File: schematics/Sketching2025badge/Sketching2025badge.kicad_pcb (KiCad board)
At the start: 2 copper layers, 100 x 100 mm, 47 parts, among them J1 Conn_02x03, J2 Conn_01x04_Pin, SW1 Capacitive_Button, SW10 SSSS811101, SW2 Capacitive_Button, SW3 Capacitive_Button, U1 ATtiny816-M

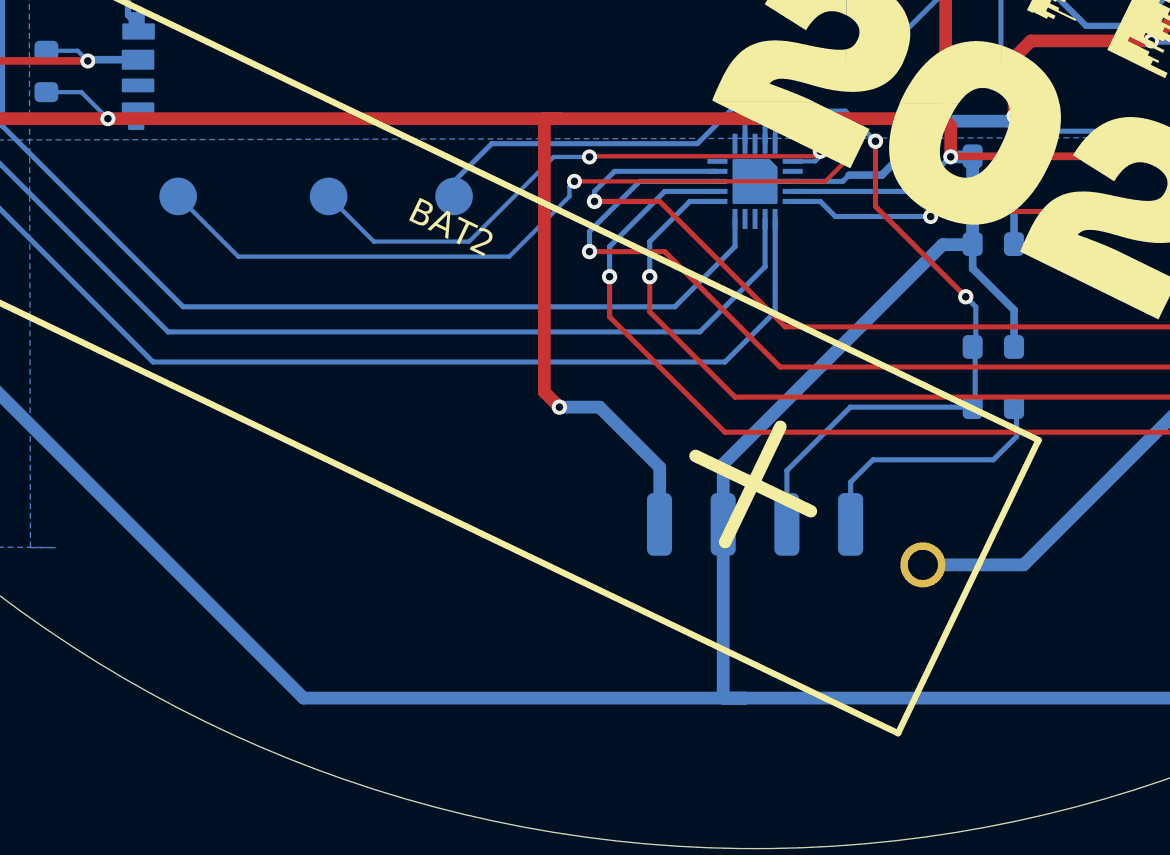
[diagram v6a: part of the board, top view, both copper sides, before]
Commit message: moved to female prog header, widened mask polygons for more light
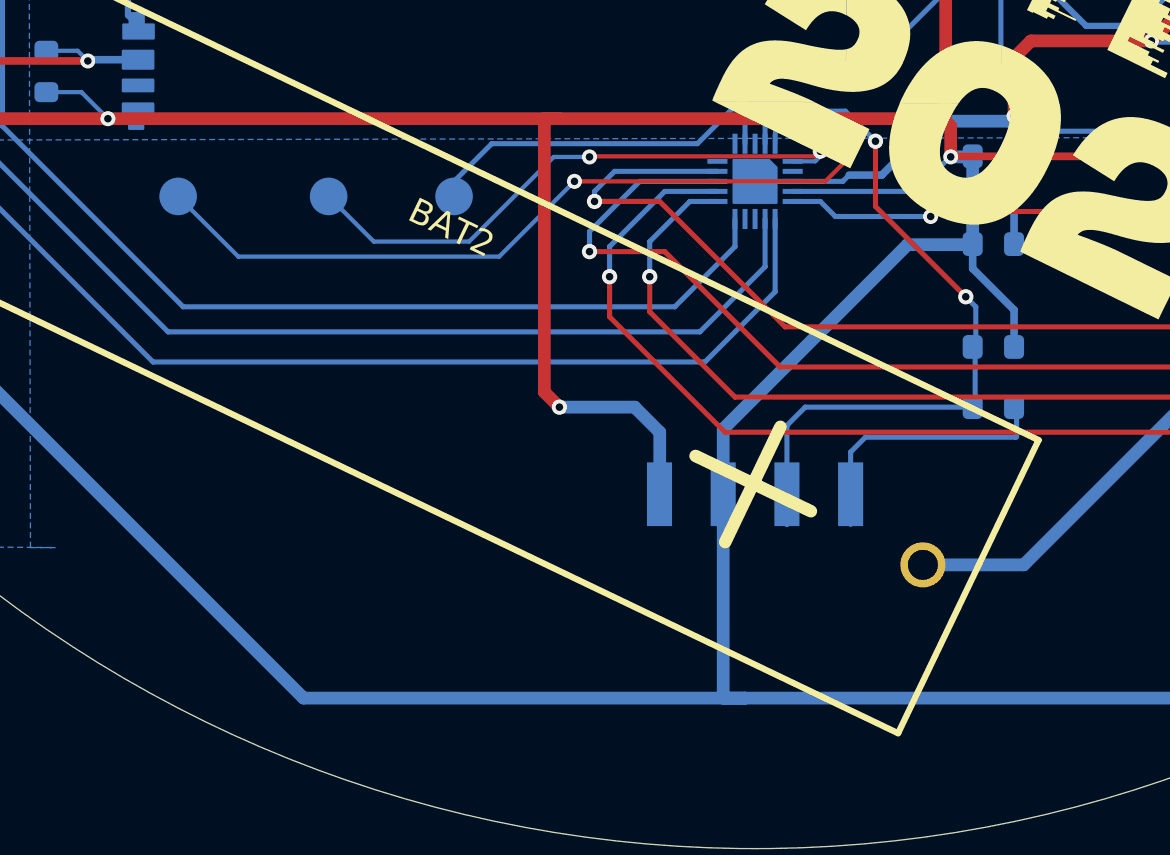
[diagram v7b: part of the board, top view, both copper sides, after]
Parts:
- removed J2: Conn_01x04_Pin, Connector_Harwin:Harwin_M20-89004xx_1x04_P2.54mm_Horizontal
- added CN1: X6511FRS-04-C85D30, easyeda2kicad:HDR-SMD_4P-P2.54-H-F, B.Cu at (100.0, 135.9)
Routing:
- net /RESET: track 28.6 -> 29.6 mm
- net VCC: track 458.6 -> 459.4 mm
- net /TX: track 10.2 -> 10.9 mm
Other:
- board text added: "tx rx V+ gnd"
- board text removed: "tx rx 3v3 gnd"

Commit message: minor fixups to pcb
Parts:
- moved LED9 4.86 mm to (76.2, 114.2)
- moved C11 4.59 mm to (73.0, 114.6)
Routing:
- net GND: track 406.9 -> 412.4 mm
- net Net-(LED8-DOUT): track 26.9 -> 21.7 mm
- net VCC: track 459.4 -> 458.5 mm
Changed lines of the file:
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@@
 	(footprint "todbot_stuff:LED-SMD_4P-L4.0-W1.6-L"
 		(layer "B.Cu")
-		(at 75.4125 119 -90)
+		(at 76.2 114.2 -90)
 		(property "Reference" "LED9"
 			(at 3.2 0.4125 180)
@@
 	(footprint "Resistor_SMD:R_0603_1608Metric"
 		(layer "B.Cu")
-		(at 71.745843 119.018187 -90)
+		(at 73 114.6 -90)
 		(descr "Resistor SMD 0603 (1608 Metric), square (rectangular) end terminal, IPC-7351 nominal, (Body size source: IPC-SM-782 page 72, https://www.pcb-3d.com/wordpress/wp-content/uploads/ipc-sm-782a_amendment_1_and_2.pdf), generated with kicad-footprint-generator")
 		(tags "resistor")
@@
 	)
 	(gr_rect
-		(start 76.9 117.4)
-		(end 97.9 120.4)
+		(start 77.3 112.6)
+		(end 97.9 115.6)
 		(stroke
 			(width 0.1)
@@
 	)
 	(segment
-		(start 92.2 120.9)
-		(end 74.2 120.9)
-		(width 0.508)
-		(layer "F.Cu")
-		(net 1)
-	)
-	(segment
 		(start 94.6 104)
 		(end 94.6 106.4)
@@
 	)
 	(segment
+		(start 92.2 120.9)
+		(end 75.4 120.9)
+		(width 0.508)
+		(layer "F.Cu")
+		(net 1)
+	)
+	(segment
 		(start 106 96.8)
 		(end 101.8 92.6)
@@
 	)
 	(segment
-		(start 92.2 120.9)
-		(end 106.19575 120.9)
+		(start 67.527876 120.9)
+		(end 65.656566 119.02869)
 		(width 0.508)
 		(layer "F.Cu")
@@
 	)
 	(segment
-		(start 74.2 120.9)
-		(end 67.527876 120.9)
+		(start 92.2 120.9)
+		(end 106.19575 120.9)
 		(width 0.508)
 		(layer "F.Cu")
@@
 	)
 	(segment
-		(start 110.326223 118.473777)
-		(end 111 117.8)
+		(start 75.4 120.9)
+		(end 67.527876 120.9)
 		(width 0.508)
 		(layer "F.Cu")
@@
 	)
 	(segment
-		(start 117.8 115.8)
-		(end 117.8 100.8)
+		(start 110.326223 118.473777)
+		(end 111 117.8)
 		(width 0.508)
 		(layer "F.Cu")
@@
 	)
 	(segment
-		(start 67.527876 120.9)
-		(end 65.656566 119.02869)
+		(start 117.8 115.8)
+		(end 117.8 100.8)
 		(width 0.508)
 		(layer "F.Cu")
@@
 	)
 	(via
-		(at 74.2 120.9)
+		(at 75.4 120.9)
 		(size 0.6)
 		(drill 0.3)
@@
 	)
 	(segment
-		(start 75.3025 120.9)
-		(end 75.4025 120.8)
-		(width 0.3048)
-		(layer "B.Cu")
-		(net 1)
-	)
-	(segment
 		(start 94.6 105.600471)
 		(end 94.498009 105.49848)
@@
 	)
 	(segment
+		(start 73.9875 117.2)
+		(end 73 116.2125)
+		(width 0.17)
+		(layer "B.Cu")
+		(net 1)
+	)
+	(segment
 		(start 105.05 123.15)
 		(end 106.29575 121.90425)
@@
 	)
 	(segment
+		(start 75.39 118.41)
+		(end 76.19 117.61)
+		(width 0.3048)
+		(layer "B.Cu")
+		(net 1)
+	)
+	(segment
 		(start 77.4 66.6)
 		(end 75.683747 68.316253)
@@
 	)
 	(segment
+		(start 76.19 117.61)
+		(end 76.19 116)
+		(width 0.3048)
+		(layer "B.Cu")
+		(net 1)
+	)
+	(segment
 		(start 99.190128 92.109885)
 		(end 100.109885 92.109885)
@@
 	)
 	(segment
+		(start 73 116.2125)
+		(end 73 115.425)
+		(width 0.17)
+		(layer "B.Cu")
+		(net 1)
+	)
+	(segment
 		(start 128.426019 80.026019)
 		(end 128.4 80)
@@
 	)
 	(segment
-		(start 71.745843 119.843187)
-		(end 73.143187 119.843187)
-		(width 0.17)
-		(layer "B.Cu")
-		(net 1)
-	)
-	(segment
 		(start 80.2025 83.2)
 		(end 71.2 83.2)
@@
 	)
 	(segment
+		(start 75.4 120.9)
+		(end 75.4 120.8225)
+		(width 0.3048)
+		(layer "B.Cu")
+		(net 1)
+	)
+	(segment
 		(start 71.2 97.8)
 		(end 73 99.6)
@@
 	)
 	(segment
+		(start 75.4 120.8225)
+		(end 75.39 120.8125)
+		(width 0.3048)
+		(layer "B.Cu")
+		(net 1)
+	)
+	(segment
 		(start 134.4 121.4)
 		(end 126.2 121.4)
@@
 	)
 	(segment
+		(start 75.39 120.8125)
+		(end 75.39 118.41)
+		(width 0.3048)
+		(layer "B.Cu")
+		(net 1)
+	)
+	(segment
 		(start 100.712166 92.712166)
 		(end 100.6 92.6)
@@
 	)
 	(segment
-		(start 74.2 120.9)
-		(end 75.3025 120.9)
-		(width 0.3048)
-		(layer "B.Cu")
-		(net 1)
-	)
-	(segment
 		(start 93.6 103.2)
 		(end 93.4 103.2)
@@
 	)
 	(segment
+		(start 76.19 117.2)
+		(end 73.9875 117.2)
+		(width 0.17)
+		(layer "B.Cu")
+		(net 1)
+	)
+	(segment
 		(start 128.4 94.2)
 		(end 120.7975 94.2)
@@
 	)
 	(segment
-		(start 73.143187 119.843187)
-		(end 74.2 120.9)
-		(width 0.17)
-		(layer "B.Cu")
-		(net 1)
-	)
-	(segment
 		(start 121.5975 117.8)
 		(end 115.8 117.8)
@@
 	)
 	(segment
-		(start 58 111.6)
-		(end 62 111.6)
+		(start 74 114.4)
+		(end 61 114.4)
+		(width 0.3048)
+		(layer "F.Cu")
+		(net 2)
+	)
+	(segment
+		(start 74.6 113.8)
+		(end 74 114.4)
 		(width 0.3048)
 		(layer "F.Cu")
@@
 	)
 	(segment
-		(start 67.8 81)
-		(end 73.6 81)
+		(start 58.2 111.6)
+		(end 58 111.6)
+		(width 0.3048)
+		(layer "F.Cu")
+		(net 2)
+	)
+	(segment
+		(start 61 114.4)
+		(end 58.2 111.6)
 		(width 0.3048)
 		(layer "F.Cu")
@@
 	)
 	(segment
-		(start 62 111.6)
-		(end 69 118.6)
+		(start 67.8 81)
+		(end 73.6 81)
 		(width 0.3048)
 		(layer "F.Cu")
@@
 	)
 	(segment
-		(start 69 118.6)
-		(end 73.4 118.6)
-		(width 0.3048)
-		(layer "F.Cu")
-		(net 2)
-	)
-	(segment
 		(start 127.2 82.6)
 		(end 127.2 96.4)
@@
 	)
 	(via
-		(at 73.4 118.6)
+		(at 74.6 113.8)
 		(size 0.6)
 		(drill 0.3)
@@
 	)
 	(segment
+		(start 74.6 113.8)
+		(end 73.025 113.8)
+		(width 0.17)
+		(layer "B.Cu")
+		(net 2)
+	)
+	(segment
 		(start 92.99 99.270826)
 		(end 93.65 99.270826)
@@
 	)
 	(segment
+		(start 73.025 113.8)
+		(end 73 113.775)
+		(width 0.17)
+		(layer "B.Cu")
+		(net 2)
+	)
+	(segment
 		(start 123.6 120.6)
 		(end 123 120)
@@
 	)
 	(segment
-		(start 73.45 118.55)
-		(end 73.4 118.6)
+		(start 74.85 113.75)
+		(end 76.19 113.75)
 		(width 0.3048)
 		(layer "B.Cu")
@@
 	)
 	(segment
-		(start 72.993187 118.193187)
-		(end 73.4 118.6)
-		(width 0.17)
-		(layer "B.Cu")
-		(net 2)
-	)
-	(segment
 		(start 142.6 106.4)
 		(end 138.025 110.975)
@@
 	)
 	(segment
-		(start 75.4025 118.55)
-		(end 73.45 118.55)
-		(width 0.3048)
-		(layer "B.Cu")
-		(net 2)
-	)
-	(segment
 		(start 93.65 99.270826)
 		(end 94.2 98.720826)
@@
 	)
 	(segment
-		(start 71.745843 118.193187)
-		(end 72.993187 118.193187)
-		(width 0.17)
-		(layer "B.Cu")
-		(net 2)
-	)
-	(segment
 		(start 123.6 122.4)
 		(end 123.6 120.6)
@@
 	)
 	(segment
+		(start 74.8 113.8)
+		(end 74.85 113.75)
+		(width 0.3048)
+		(layer "B.Cu")
+		(net 2)
+	)
+	(segment
 		(start 133.2 129.515795)
 		(end 131.888154 128.203949)
@@
 	)
 	(segment
+		(start 74.6 113.8)
+		(end 74.8 113.8)
+		(width 0.3048)
+		(layer "B.Cu")
+		(net 2)
+	)
+	(segment
 		(start 67.8 81)
 		(end 61.5 81)
@@
 	)
 	(segment
-		(start 81.8 99.4)
-		(end 80.4 100.8)
+		(start 75.8 106)
+		(end 76.21 106.41)
 		(width 0.25)
 		(layer "B.Cu")
@@
 	)
 	(segment
-		(start 78 100.8)
-		(end 75 103.8)
+		(start 75.8 103)
+		(end 75.8 106)
 		(width 0.25)
 		(layer "B.Cu")
@@
 	)
 	(segment
-		(start 75 103.8)
-		(end 75 116.7775)
+		(start 81.8 96.4)
+		(end 81.8 99.4)
 		(width 0.25)
 		(layer "B.Cu")
@@
 	)
 	(segment
-		(start 81.8 96.4)
-		(end 81.8 99.4)
+		(start 81.8 99.4)
+		(end 80.4 100.8)
 		(width 0.25)
 		(layer "B.Cu")
@@
 	)
 	(segment
-		(start 80.4025 95.77)
-		(end 81.17 95.77)
+		(start 81.17 95.77)
+		(end 81.8 96.4)
 		(width 0.25)
 		(layer "B.Cu")
@@
 	)
 	(segment
-		(start 81.17 95.77)
-		(end 81.8 96.4)
+		(start 78 100.8)
+		(end 75.8 103)
 		(width 0.25)
 		(layer "B.Cu")
@@
 	)
 	(segment
-		(start 75 116.7775)
-		(end 75.4225 117.2)
+		(start 76.21 106.41)
+		(end 76.21 112.4)
 		(width 0.25)
 		(layer "B.Cu")
@@
 		(width 0.25)
 		(layer "B.Cu")
+		(net 32)
+	)
+	(segment
+		(start 80.4025 95.77)
+		(end 81.17 95.77)
+		(width 0.25)
+		(layer "B.Cu")
